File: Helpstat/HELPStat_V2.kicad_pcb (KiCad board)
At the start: 2 copper layers, 61.8 x 44.4 mm, 65 parts, among them IC1 MCP73831/OT, Q1 2.5A/30V/105mΩ

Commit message: Andrew Edits
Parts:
- added C10: 470n, Capacitor_SMD:C_0402_1005Metric, F.Cu at (102.1, 90.0)
- added C11: 4.7u, Capacitor_SMD:C_0402_1005Metric, F.Cu at (104.9, 84.1)
- added C12: 470n, Capacitor_SMD:C_0402_1005Metric, F.Cu at (104.9, 86.1)
- added C17: 10u, Capacitor_SMD:C_0402_1005Metric, F.Cu at (104.9, 88.0)
- added C18: 100n, Capacitor_SMD:C_0402_1005Metric, F.Cu at (104.9, 90.0)
- added C19: 100n, Capacitor_SMD:C_0402_1005Metric, F.Cu at (107.8, 84.1)
- added C20: 100n, Capacitor_SMD:C_0402_1005Metric, F.Cu at (107.8, 86.1)
- added C21: 100n, Capacitor_SMD:C_0402_1005Metric, F.Cu at (107.8, 88.0)
- added C22: 100n, Capacitor_SMD:C_0402_1005Metric, F.Cu at (107.8, 90.0)
- added C3: 10u, Capacitor_SMD:C_0402_1005Metric, F.Cu at (99.2, 84.1)
- added C4: 10u, Capacitor_SMD:C_0402_1005Metric, F.Cu at (99.2, 86.1)
- added C5: 10u, Capacitor_SMD:C_0402_1005Metric, F.Cu at (99.2, 88.0)
- added C6: 10u, Capacitor_SMD:C_0402_1005Metric, F.Cu at (99.2, 90.0)
- added C7: 1u, Capacitor_SMD:C_0402_1005Metric, F.Cu at (102.1, 84.1)
- added C8: 470n, Capacitor_SMD:C_0402_1005Metric, F.Cu at (102.1, 86.1)
- added C9: 470n, Capacitor_SMD:C_0402_1005Metric, F.Cu at (102.1, 88.0)
- added D1: BAT20JFILM, BAT20JFILM:SOD-323, F.Cu at (99.7, 110.9)
- added J1: 10118192-0001LF, 10118192_0001LF:AMPHENOL_10118192-0001LF, F.Cu at (103.2, 76.9)
- added R4: 100k, Resistor_SMD:R_0603_1608Metric, F.Cu at (105.3, 106.2)
- added R7: 4k7, Resistor_SMD:R_0402_1005Metric, F.Cu at (109.0, 92.0)
- added R8: 4k7, Resistor_SMD:R_0402_1005Metric, F.Cu at (109.0, 94.0)
- added R9: 4k7, Resistor_SMD:R_0402_1005Metric, F.Cu at (109.0, 96.0)
- added U1: ESP32-DEVKITC-32D, ESP32-DEVKITC-32D:MODULE_ESP32-DEVKITC-32D, F.Cu at (83.0, 102.8)
- added U2: MCP73831T-2ACI/OT, MCP73831T_2ACI_OT:SOT-23-5_MC_MCH, F.Cu at (100.6, 107.3)
- added U3: AP2112K-3.3TRG1, AP2112K_3_3TRG1:SOT95P285X140-5N, F.Cu at (100.9, 102.6)
- added U4: AD5941BCPZ-RL7, AD5941BCPZ_RL7:QFN50P700X700X80-49N, F.Cu at (103.0, 95.6)

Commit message: Sch Draft Completed
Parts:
- added CS0: TestPoint_Alt, TestPoint:TestPoint_Pad_2.0x2.0mm, F.Cu at (129.0, 87.1)
- added H2: MOUNT-HOLE2.2, MountingHole:MountingHole_2.2mm_M2_Pad, F.Cu at (115.6, 105.3)
- added H4: MOUNT-HOLE2.2, MountingHole:MountingHole_2.2mm_M2_Pad, F.Cu at (115.6, 111.2)
- added I2C0: M50-3530442, M50_3530442:HARWIN_M50-3530442, F.Cu at (116.5, 82.2)
- added J2: LIPO1, B2B_XH_A:JST_B2B-XH-A, F.Cu at (126.9, 117.8)
- added J3: M20-9990246, M20_9990246:HARWIN_M20-9990246, F.Cu at (123.6, 82.4)
- added J4: M20-9990246, M20_9990246:HARWIN_M20-9990246, F.Cu at (123.6, 86.5)
- added J5: M20-9990246, M20_9990246:HARWIN_M20-9990246, F.Cu at (123.6, 90.6)
- added J6: M50-3530442, M50_3530442:HARWIN_M50-3530442, F.Cu at (116.5, 85.9)
- added J7: M50-3530442, M50_3530442:HARWIN_M50-3530442, F.Cu at (116.5, 89.5)
- added J8: M50-3530442, M50_3530442:HARWIN_M50-3530442, F.Cu at (116.5, 93.2)
- added LED1: YLW, LED1212_AndrewCustom:LED_00-R18_OSR, F.Cu at (121.0, 104.6)
- added LED2: GRN, LED1212_AndrewCustom:LED_00-R18_OSR, F.Cu at (121.0, 109.3)
- added MOSFET1: BSS205NH6327XTSA1, BSS205NH6327XTSA1:PG-SOT23-3-5_INF, F.Cu at (129.3, 131.9)
- added SPI0: M50-3530442, M50_3530442:HARWIN_M50-3530442, F.Cu at (116.5, 96.8)
- added TP1: TestPoint, TestPoint:TestPoint_Pad_D1.0mm, F.Cu at (124.9, 103.8)
- added TP2: TestPoint, TestPoint:TestPoint_Pad_D1.0mm, F.Cu at (124.9, 106.9)
- added TP3: TestPoint, TestPoint:TestPoint_Pad_D1.0mm, F.Cu at (127.9, 103.8)
- added TP4: TestPoint, TestPoint:TestPoint_Pad_D1.0mm, F.Cu at (127.9, 106.9)
- added TP5: TestPoint, TestPoint:TestPoint_Pad_D1.0mm, F.Cu at (131.0, 103.8)
- added TP6: TestPoint, TestPoint:TestPoint_Pad_D1.0mm, F.Cu at (131.0, 106.9)
- added UART0: M50-3530442, M50_3530442:HARWIN_M50-3530442, F.Cu at (116.5, 100.5)
- moved J1 50.8 mm to (118.1, 125.5)
- moved R7 37.2 mm to (127.3, 124.5)
- moved R8 37.2 mm to (127.3, 126.5)
- moved R9 37.2 mm to (127.3, 128.5)
- moved U3 35.3 mm to (130.1, 82.7)
- moved D1 33.9 mm to (130.7, 124.7)
- moved R4 28.4 mm to (128.9, 90.4)
- moved AD5941 28.2 mm to (185.0, 106.2)
- moved BOOT0 28.2 mm to (156.9, 92.2)
- moved C1 28.2 mm to (160.1, 116.5)
- moved C11 28.2 mm to (192.1, 106.1)
- moved C17 28.2 mm to (205.1, 88.3)
- moved C19 28.2 mm to (205.1, 86.9)
- moved C5 28.2 mm to (158.1, 115.7)
- moved C7 28.2 mm to (156.7, 115.7)
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
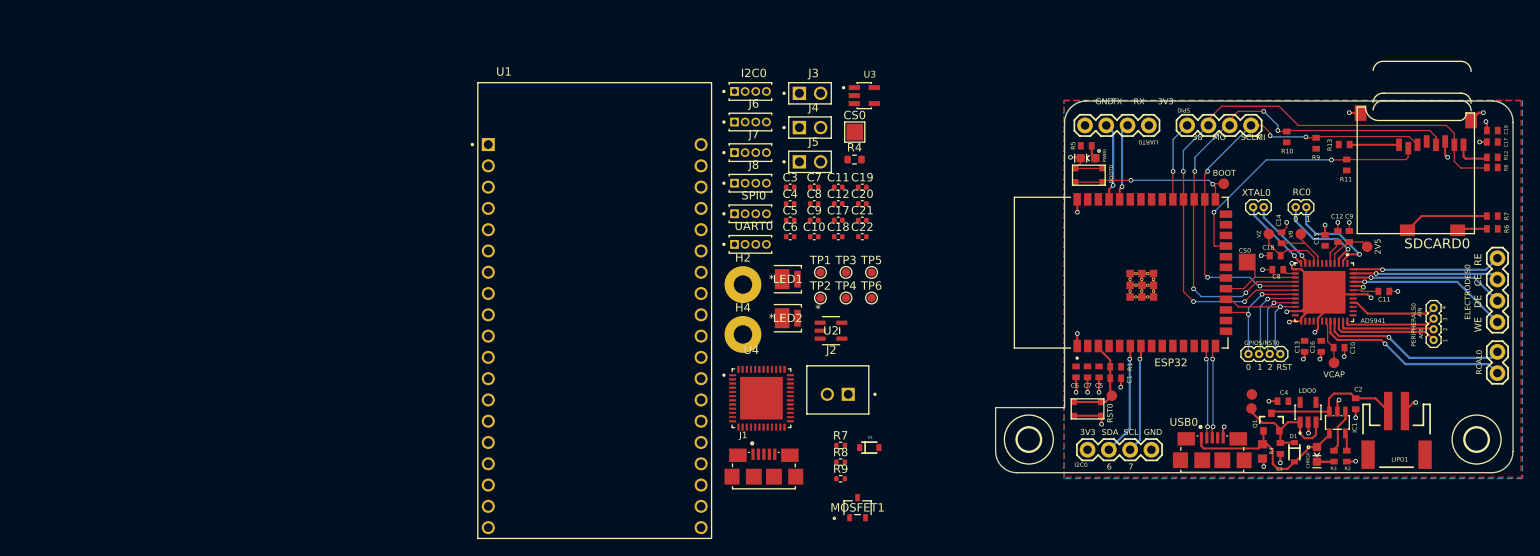
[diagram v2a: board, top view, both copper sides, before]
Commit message: added firmware template and pcb
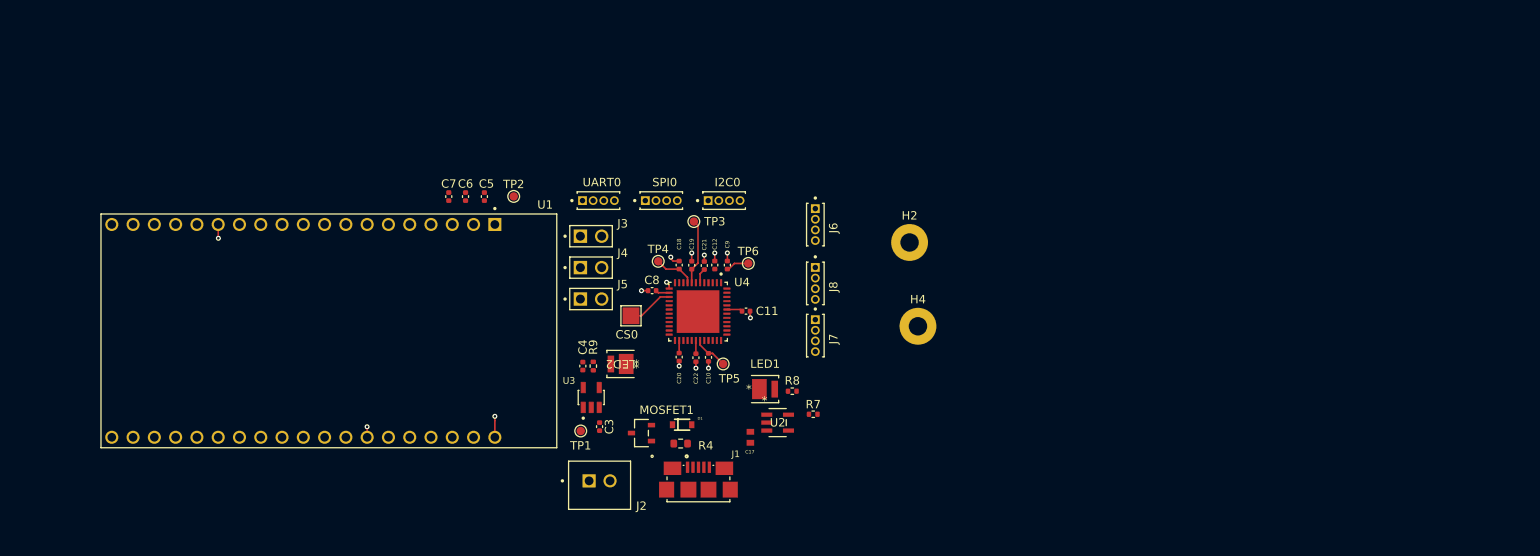
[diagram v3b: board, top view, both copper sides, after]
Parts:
- removed AD5941: AD5941BCPZ-RL7, QFN50P700X700X80-49N_39313983
- removed BOOT0, RST0: , BUTTON-GULLWING
- removed C1, C2: 10u, C0402
- removed the C10 at (186.8, 112.8)
- removed the C11 at (192.1, 106.1)
- removed the C12 at (186.6, 99.5)
- removed C13, C14, C15, C16: 100n, C0402
- removed the C17 at (127.0, 97.6)
- removed the C18 at (179.1, 101.8)
- removed the C19 at (205.1, 86.9)
- removed the C3 at (179.8, 124.8)
- removed the C4 at (180.1, 119.2)
- removed the C5 at (158.1, 115.7)
- removed the C6 at (155.4, 115.7)
- removed the C7 at (156.7, 115.7)
- removed the C8 at (179.5, 103.5)
- removed the C9 at (188.0, 99.5)
- removed CHRG0: YLW, LED-0603
- removed the CS0 at (175.8, 102.6)
- removed the D1 at (181.4, 125.3)
- removed ELECTRODES0: , 1X04
- removed ESP32: ESP32-S3-WROOM-1-N8R8, XCVR_ESP32S3WROOM1N8R8
- removed GPIOS/RST0, PERIPHERALS0: , 1X04_1.27MM
- removed the H2 at (149.7, 123.8)
- removed the H4 at (203.2, 123.8)
- removed the I2C0 at (156.7, 125.0)
- removed IC1: MCP73831/OT, SOT23-5L
- removed LDO0: AP2112K-3.3TRG1, SOT95P285X140-5N_39313995
- removed LIPO1: , JST-2-SMD
- removed PWR0: GREEN, LED-0603
- removed Q1: 2.5A/30V/105mΩ, SOT23-3
- removed R1: 10k, R0402
- removed R10, R11, R12, R13, R6: 47k, R0402
- removed R2, R3, R5: 4k7, R0402
- removed the R4 at (177.6, 125.2)
- removed the R7 at (205.1, 97.1)
- removed the R8 at (205.1, 91.3)
- removed the R9 at (184.0, 88.4)
- removed RC0, XTAL0: , 1X02_1.27MM
- removed RCAL0: , 1X02
- removed SDCARD0: MICROSD, MICROSD
- removed the SPI0 at (168.6, 86.3)
- removed the TP1 at (173.0, 93.2)
- removed the TP2 at (159.6, 118.5)
- removed the TP3 at (176.3, 120.1)
- removed the TP4 at (176.4, 118.4)
- removed the UART0 at (164.1, 86.3)
- removed UNK2V5, VB0, VCAP0, VZ0: , PAD.03X.05
- removed USB0: 10118192-0001LF, AMPHENOL_10118192-0001LF_39346738
- moved C17 95.3 mm to (116.5, 123.5), turned to -90 degrees
- moved U3 48.6 mm to (97.5, 118.8), turned to 90 degrees
- moved C7 43.6 mm to (80.5, 94.8), turned to 90 degrees
- moved R4 39.7 mm to (108.2, 124.2), turned to 180 degrees
- moved C6 39.0 mm to (82.5, 94.8), turned to 90 degrees
- moved TP2 38.6 mm to (88.2, 94.8)
- moved C5 36.6 mm to (84.8, 94.8), turned to 90 degrees
- moved C3 36.5 mm to (98.5, 122.2), turned to -90 degrees
- moved CS0 34.5 mm to (102.2, 109.0)
- moved TP1 34.3 mm to (96.2, 122.8)
- moved R9 32.4 mm to (97.8, 115.0), turned to 90 degrees
- moved U1 31.8 mm to (66.2, 110.8), turned to -90 degrees
- moved C4 31.4 mm to (96.5, 115.0), turned to 90 degrees
- moved J3 31.2 mm to (97.5, 99.5)
- moved J4 31.0 mm to (97.5, 103.2)
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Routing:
- net GND: track 95.5 -> 15.1 mm, vias 38 -> 14
- net MISO: track 75.1 -> 0.00 mm, vias 3 -> 0
- net SCLK: track 63.1 -> 0.00 mm, vias 5 -> 0
- net MOSI: track 52.8 -> 0.00 mm, vias 5 -> 0
- net CS.SD: track 32.4 -> 0.00 mm, vias 2 -> 0
- net RCAL0: track 23.3 -> 0.00 mm, vias 1 -> 0
- net V_USB: track 22.3 -> 0.00 mm
- net RCAL1: track 22.3 -> 0.00 mm, vias 1 -> 0
- net BOOT: track 20.0 -> 0.00 mm, vias 2 -> 0
- net WE: track 19.2 -> 0.00 mm, vias 1 -> 0
- net DE: track 18.4 -> 0.00 mm, vias 1 -> 0
- net RE: track 17.8 -> 0.00 mm, vias 1 -> 0
- net CE: track 17.5 -> 0.00 mm, vias 1 -> 0
- net VLIPO: track 16.7 -> 0.00 mm
- net N$7: track 16.1 -> 0.00 mm
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- removed copper zone on F.Cu, net 3.3V
- removed copper zone on B.Cu, net GND
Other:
- board outline removed
- board text removed: "0"
- board text removed: "1"
- board text removed: "2"
- board text removed: "2V5"
- board text removed: "3"
- board text removed: "38"
- board text removed: "3V3"
- board text removed: "4"
- board text removed: "6"
- board text removed: "7"
- board text removed: "AFE"
- board text removed: "AIN"
- board text removed: "BOOT"
- board text removed: "CE"
- board text removed: "DE"
- board text removed: "GND"
- board text removed: "MI"
- board text removed: "MO"
- board text removed: "RE"
- board text removed: "RST"
- board text removed: "RX"
- board text removed: "SCL"
- board text removed: "SCLK"
- board text removed: "SDA"
- board text removed: "TX"
- board text removed: "VB"
- board text removed: "VCAP"
- board text removed: "VZ"
- board text removed: "WE"

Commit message: more pcb changes
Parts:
- moved I2C0 59.7 mm to (53.6, 94.5), turned to 180 degrees
- moved SPI0 56.2 mm to (59.9, 127.5)
- moved UART0 38.4 mm to (77.5, 127.5)
- moved J3 29.1 mm to (124.0, 111.5), turned to 90 degrees
- moved J6 25.6 mm to (104.5, 114.4)
- moved CS0 22.9 mm to (120.0, 94.5)
- moved J5 20.9 mm to (114.2, 94.5)
- moved J4 12.6 mm to (106.5, 94.5), turned to 180 degrees
- moved TP1 10.1 mm to (105.8, 119.5), turned to 180 degrees
- moved C17 7.25 mm to (118.2, 130.5)
- moved U2 7.25 mm to (121.5, 128.8)
- moved LED1 7.25 mm to (120.0, 124.8)
- moved R7 7.25 mm to (125.7, 127.8)
- moved R8 7.25 mm to (123.2, 125.0)
- moved C3 6.33 mm to (104.1, 119.2), turned to 90 degrees
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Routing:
- net /MISO: track 0.00 -> 60.1 mm, vias 0 -> 1
- net /SCLK: track 0.00 -> 57.4 mm, vias 0 -> 1
- net /MOSI: track 0.00 -> 53.3 mm, vias 0 -> 1
- net /USB_P: track 0.00 -> 32.7 mm, vias 0 -> 1
- net /USB_N: track 0.00 -> 29.8 mm, vias 0 -> 1
- net VLIPO: track 0.00 -> 22.3 mm, vias 0 -> 2
- net Net-(MOSFET1-S): track 0.00 -> 19.3 mm
- net VUSB: track 0.00 -> 18.6 mm
- net /CS.SPI: track 0.00 -> 17.6 mm
- net /RCAL1: track 0.00 -> 15.2 mm, vias 0 -> 1
- net /RCAL0: track 0.00 -> 15.1 mm, vias 0 -> 1
- net GND: track 15.1 -> 29.1 mm, vias 14 -> 24
- net /RC0.1: track 0.00 -> 12.5 mm, vias 0 -> 1
- net /RC0.0: track 0.00 -> 12.1 mm, vias 0 -> 1
- net /RE: track 0.00 -> 11.6 mm
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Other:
- board outline added: 102 x 45 mm

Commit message: PCB Touches
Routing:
- net 3.3V: track 5.67 -> 135.3 mm
- net /CS.AFE: track 0.00 -> 79.6 mm, vias 0 -> 1
- net /AFE.RST: track 7.18 -> 63.0 mm, vias 0 -> 2
- net /GPIO.0: track 4.87 -> 48.9 mm, vias 0 -> 1
- net VLIPO: track 22.3 -> 31.4 mm
- added copper zone on B.Cu, net GND
- added copper zone on F.Cu, net GND

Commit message: PCB Editted Routes
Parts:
- moved C20 0.27 mm to (107.8, 114.0)
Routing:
- net 3.3V: track 135.3 -> 167.7 mm, vias 0 -> 1
- net VUSB: track 18.6 -> 32.7 mm, vias 0 -> 2
- net GND: track 29.1 -> 29.7 mm
- net /BIAS.0: track 7.32 -> 7.82 mm
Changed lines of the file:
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@@
 	(footprint "Capacitor_SMD:C_0402_1005Metric"
 		(layer "F.Cu")
-		(at 108 113.925 -90)
+		(at 107.75 114.02 -90)
 		(descr "Capacitor SMD 0402 (1005 Metric), square (rectangular) end terminal, IPC_7351 nominal, (Body size source: IPC-SM-782 page 76, https://www.pcb-3d.com/wordpress/wp-content/uploads/ipc-sm-782a_amendment_1_and_2.pdf), generated with kicad-footprint-generator")
 		(tags "capacitor")
@@
 	)
 	(segment
-		(start 108 114.405)
-		(end 108 115)
-		(width 0.2)
-		(layer "F.Cu")
-		(net 1)
-	)
-	(segment
 		(start 118.700001 128.799999)
 		(end 118.5 129)
@@
 	)
 	(segment
+		(start 107.75 114.5)
+		(end 107.75 115.360781)
+		(width 0.2)
+		(layer "F.Cu")
+		(net 1)
+	)
+	(segment
 		(start 118.449999 131.199999)
 		(end 119.25 132)
@@
 	)
 	(segment
+		(start 107.75 115.360781)
+		(end 107.5 115.610781)
+		(width 0.2)
+		(layer "F.Cu")
+		(net 1)
+	)
+	(segment
 		(start 113.75 101.965)
 		(end 113.75 101)
@@
 	)
 	(via
-		(at 108 115)
+		(at 107.5 115.610781)
 		(size 0.6)
 		(drill 0.3)
@@
 	(segment
 		(start 110.5 103.48)
-		(end 110.5 105.055)
+		(end 110.5 104.25)
+		(width 0.2)
+		(layer "F.Cu")
+		(net 2)
+	)
+	(segment
+		(start 110.015 104.25)
+		(end 110 104.235)
 		(width 0.2)
 		(layer "F.Cu")
@@
 	)
 	(segment
+		(start 108.5 114.27)
+		(end 108.48 114.27)
+		(width 0.2)
+		(layer "F.Cu")
+		(net 2)
+	)
+	(segment
 		(start 85.25 95.25)
 		(end 85.75 94.75)
@@
 	)
 	(segment
-		(start 113.75 117.5)
+		(start 110.5 104.25)
+		(end 110.5 105.055)
+		(width 0.2)
+		(layer "F.Cu")
+		(net 2)
+	)
+	(segment
+		(start 108.5 114.27)
+		(end 109.25 113.52)
+		(width 0.2)
+		(layer "F.Cu")
+		(net 2)
+	)
+	(segment
+		(start 108.5 117.5)
 		(end 97 117.5)
 		(width 0.2)
@@
 	)
 	(segment
+		(start 113.75 117.5)
+		(end 108.5 117.5)
+		(width 0.2)
+		(layer "F.Cu")
+		(net 2)
+	)
+	(segment
 		(start 79.75 94.5)
 		(end 80.5 95.25)
@@
 	)
 	(segment
+		(start 108.5 117.5)
+		(end 108.5 114.27)
+		(width 0.2)
+		(layer "F.Cu")
+		(net 2)
+	)
+	(segment
 		(start 95.5 114.73)
 		(end 77.27 114.73)
@@
 	)
 	(segment
+		(start 110.5 104.25)
+		(end 110.015 104.25)
+		(width 0.2)
+		(layer "F.Cu")
+		(net 2)
+	)
+	(segment
 		(start 75.595 127.5)
 		(end 74.75 126.655)
@@
 	)
 	(segment
+		(start 108.48 114.27)
+		(end 107.75 113.54)
+		(width 0.2)
+		(layer "F.Cu")
+		(net 2)
+	)
+	(segment
 		(start 85.75 94.75)
 		(end 88.25 94.75)
@@
 		(net 2)
 	)
+	(via
+		(at 110 104.235)
+		(size 0.6)
+		(drill 0.3)
+		(layers "F.Cu" "B.Cu")
+		(net 2)
+	)
+	(segment
+		(start 110 104.235)
+		(end 109.985 104.25)
+		(width 0.2)
+		(layer "B.Cu")
+		(net 2)
+	)
+	(segment
+		(start 109.985 104.25)
+		(end 106.75 104.25)
+		(width 0.2)
+		(layer "B.Cu")
+		(net 2)
+	)
+	(segment
+		(start 106.5 104)
+		(end 105.5 104)
+		(width 0.2)
+		(layer "B.Cu")
+		(net 2)
+	)
+	(segment
+		(start 99.6 98.1)
+		(end 86 98.1)
+		(width 0.2)
+		(layer "B.Cu")
+		(net 2)
+	)
+	(segment
+		(start 105.5 104)
+		(end 99.6 98.1)
+		(width 0.2)
+		(layer "B.Cu")
+		(net 2)
+	)
+	(segment
+		(start 106.75 104.25)
+		(end 106.5 104)
+		(width 0.2)
+		(layer "B.Cu")
+		(net 2)
+	)
 	(segment
 		(start 65.68 123.59)
@@
 	)
 	(segment
+		(start 122.0073 126.7573)
+		(end 122 126.75)
+		(width 0.2)
+		(layer "F.Cu")
+		(net 38)
+	)
+	(segment
 		(start 107.5 122.75)
 		(end 105.75 122.75)
@@
 	)
 	(segment
+		(start 122 126.75)
+		(end 120.25 126.75)
+		(width 0.2)
+		(layer "F.Cu")
+		(net 38)
+	)
+	(segment
 		(start 123.7146 125.049999)
-		(end 121.8886 126.875999)
+		(end 122.0073 126.7573)
 		(width 0.2)
 		(layer "F.Cu")
@@
 	)
 	(segment
+		(start 111 124.25)
+		(end 109 124.25)
+		(width 0.2)
+		(layer "F.Cu")
+		(net 38)
+	)
+	(segment
 		(start 105.75 122.893801)
 		(end 104.6938 123.950001)
@@
 	)
 	(segment
+		(start 111.25 124.5)
+		(end 111 124.25)
+		(width 0.2)
+		(layer "F.Cu")
+		(net 38)
+	)
+	(segment
 		(start 109.5 122)
 		(end 108.25 122)
@@
 	)
 	(segment
+		(start 122.0073 126.7573)
+		(end 121.8886 126.875999)
+		(width 0.2)
+		(layer "F.Cu")
+		(net 38)
+	)
+	(via
+		(at 111.25 124.5)
+		(size 0.6)
+		(drill 0.3)
+		(layers "F.Cu" "B.Cu")
+		(net 38)
+	)
+	(via
+		(at 120.25 126.75)
+		(size 0.6)
+		(drill 0.3)
+		(layers "F.Cu" "B.Cu")
+		(net 38)
+	)
+	(segment
+		(start 120.25 126.75)
+		(end 113.5 126.75)
+		(width 0.2)
+		(layer "B.Cu")
+		(net 38)
+	)
+	(segment
+		(start 113.5 126.75)
+		(end 111.25 124.5)
+		(width 0.2)
+		(layer "B.Cu")
+		(net 38)
+	)
+	(segment
 		(start 122.799999 127.799999)
 		(end 122.75 127.849998)
@@
 	)
 	(segment
-		(start 109.5 103.445)
-		(end 109.5 105.055)
+		(start 110.25 98.25)
+		(end 110.25 102.195)
 		(width 0.2)
 		(layer "F.Cu")
@@
 	)
 	(segment
-		(start 110.25 98.25)
-		(end 110.25 102.195)
+		(start 109.5 105.055)
+		(end 109.5 102.945)
 		(width 0.2)
 		(layer "F.Cu")
@@
 	)
 	(segment
-		(start 108 104.25)
-		(end 108.25 104)
-		(width 0.2)
-		(layer "F.Cu")
-		(net 76)
-	)
-	(segment
-		(start 108 105.055)
-		(end 108 104.25)
+		(start 108 103.75)
+		(end 108 105.055)
 		(width 0.2)
 		(layer "F.Cu")
@@
 	)
 	(via
-		(at 108.25 104)
+		(at 108 103.75)
 		(size 0.6)
 		(drill 0.3)
@@
 	)
 	(segment
-		(start 108.25 104)
+		(start 108 103.75)
 		(end 107.77 103.52)
 		(width 0.2)
@@
 	)
 	(segment
+		(start 107.5 104)
+		(end 107.25 103.75)
+		(width 0.2)
+		(layer "F.Cu")
+		(net 80)
+	)
+	(segment
 		(start 107.5 105.055)
 		(end 107.5 104)
@@
 	)
 	(via
-		(at 107.5 104)
+		(at 107.25 103.75)
 		(size 0.6)
 		(drill 0.3)
@@
 	)
 	(segment
-		(start 107.5 104)
+		(start 107.25 103.75)
 		(end 105.23 101.73)
 		(width 0.2)

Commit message: Gibby Bub
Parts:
- added _: LOGO, Dome:Dome of Protection, F.Cu at (129.5, 120.0)

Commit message: pcb v2
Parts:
- removed U1: ESP32-DEVKITC-32D, ESP32-DEVKITC-32D:MODULE_ESP32-DEVKITC-32D
- added H1: MOUNT-HOLE2.2, MountingHole:MountingHole_2.2mm_M2_Pad, F.Cu at (39.0, 93.0)
- added H3: MOUNT-HOLE2.2, MountingHole:MountingHole_2.2mm_M2_Pad, F.Cu at (38.5, 131.0)
- added U5: ESP32-S3-DEVKITC-1-N8R2, ESP32-S3-DEVKITC-1-N8R2:XCVR_ESP32-S3-DEVKITC-1-N8R2, F.Cu at (60.4, 111.1)
- C10, C11, C12, C18, C19, C20, C21, C22, C3, C4, C5, C6, C7, C8, C9: footprint Capacitor_SMD:C_0402_1005Metric -> Capacitor_SMD:C_0603_1608Metric
- C17: footprint C0402 -> Capacitor_SMD:C_0603_1608Metric
- R7, R8, R9: footprint Resistor_SMD:R_0402_1005Metric -> Resistor_SMD:R_0603_1608Metric
- moved CS0 25.1 mm to (97.0, 104.5)
- moved H4 20.7 mm to (134.0, 131.0)
- moved UART0 9.36 mm to (86.9, 127.5)
- moved H2 9.34 mm to (134.0, 93.5)
- moved TP4 4.53 mm to (101.0, 102.5)
- moved C19 3.23 mm to (108.7, 99.3), turned to 180 degrees
- moved C12 3.12 mm to (112.3, 99.3), turned to 0 degrees
- moved SPI0 3.00 mm to (62.9, 127.5), turned to 180 degrees
- moved R7 2.86 mm to (124.0, 125.5)
- moved TP5 2.50 mm to (114.0, 117.0)
- moved TP3 2.26 mm to (107.5, 97.5)
- moved C10 2.15 mm to (112.5, 115.0), turned to 0 degrees
- moved R8 2.02 mm to (124.5, 123.5)
- moved TP1 1.23 mm to (107.0, 119.5)
- moved _ 1.12 mm to (129.0, 119.0)
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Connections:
- C17 pad 1: 3.3V -> VLIPO
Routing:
- net 3.3V: track 167.7 -> 124.3 mm, vias 1 -> 3
- net /USB_N: track 29.8 -> 72.4 mm, vias 1 -> 2
- net /USB_P: track 32.7 -> 70.8 mm
- net GND: track 29.7 -> 65.9 mm, vias 24 -> 16
- net /SDA/6/CH0: track 4.12 -> 25.6 mm
- net /SCL/7/CH1: track 4.66 -> 24.2 mm
- net /CS.AFE: track 79.6 -> 60.1 mm
- net /CS.SPI: track 17.6 -> 6.12 mm
- net /GPIO.0: track 48.9 -> 60.3 mm
- net /MISO: track 60.1 -> 53.4 mm, vias 1 -> 0
- net /MOSI: track 53.3 -> 58.5 mm, vias 1 -> 0
- net VUSB: track 32.7 -> 37.7 mm, vias 2 -> 0
- net /ZERO.0: track 5.43 -> 9.94 mm, vias 0 -> 2
- net /AFE.RST: track 63.0 -> 67.4 mm, vias 2 -> 1
- net /AVDD.REG: track 2.65 -> 5.93 mm
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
